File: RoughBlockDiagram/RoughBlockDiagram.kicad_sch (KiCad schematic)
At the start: 11 parts, among them J1 IEC_60320_C14_Receptacle, P1 Conn_Plug_3P_Protected, U1 RaspberryPi, U2 Arduino, U3 Encoder Driver

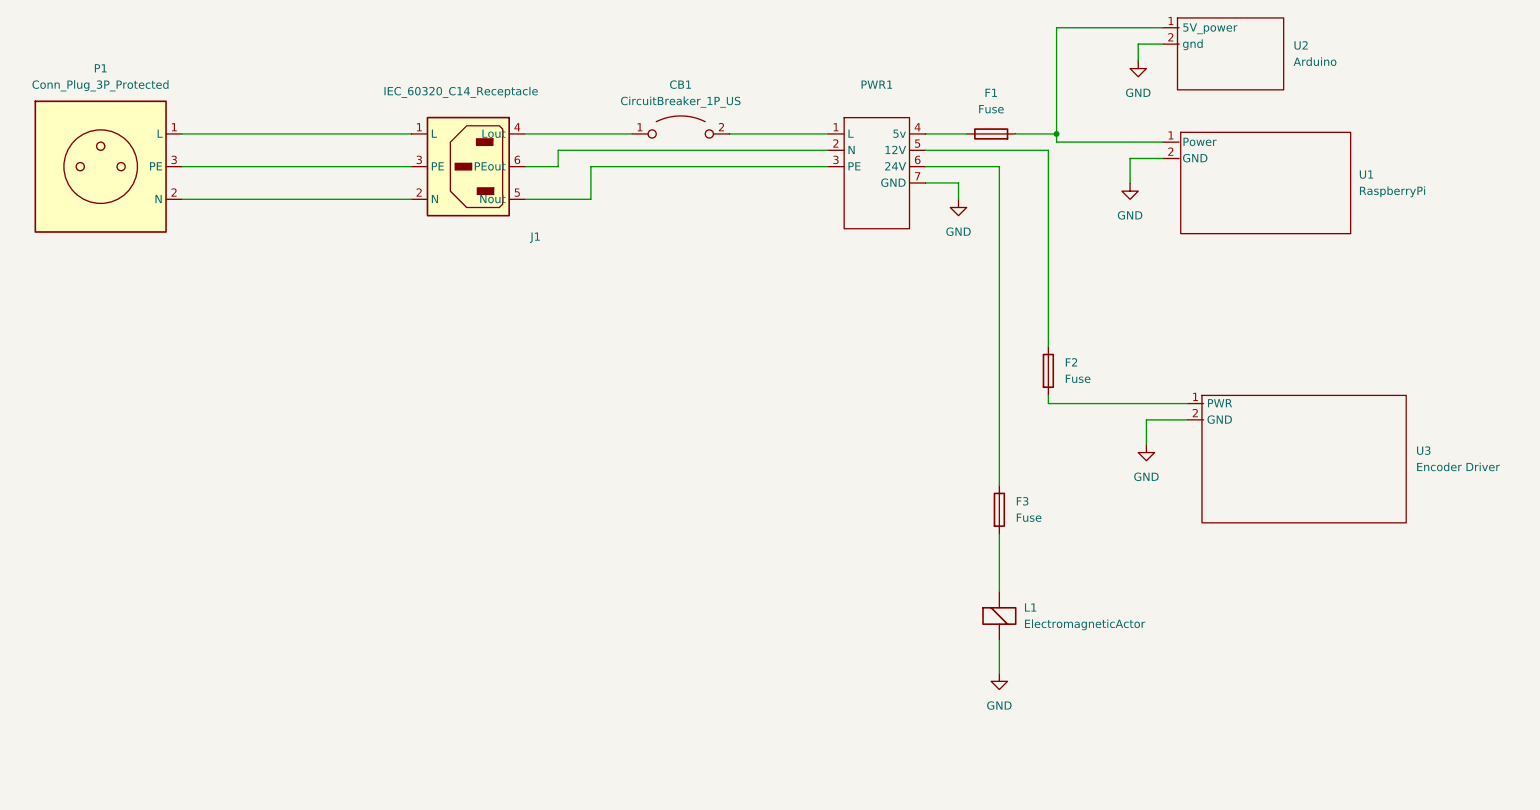
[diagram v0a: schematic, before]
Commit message: Block diagram schematic updated.
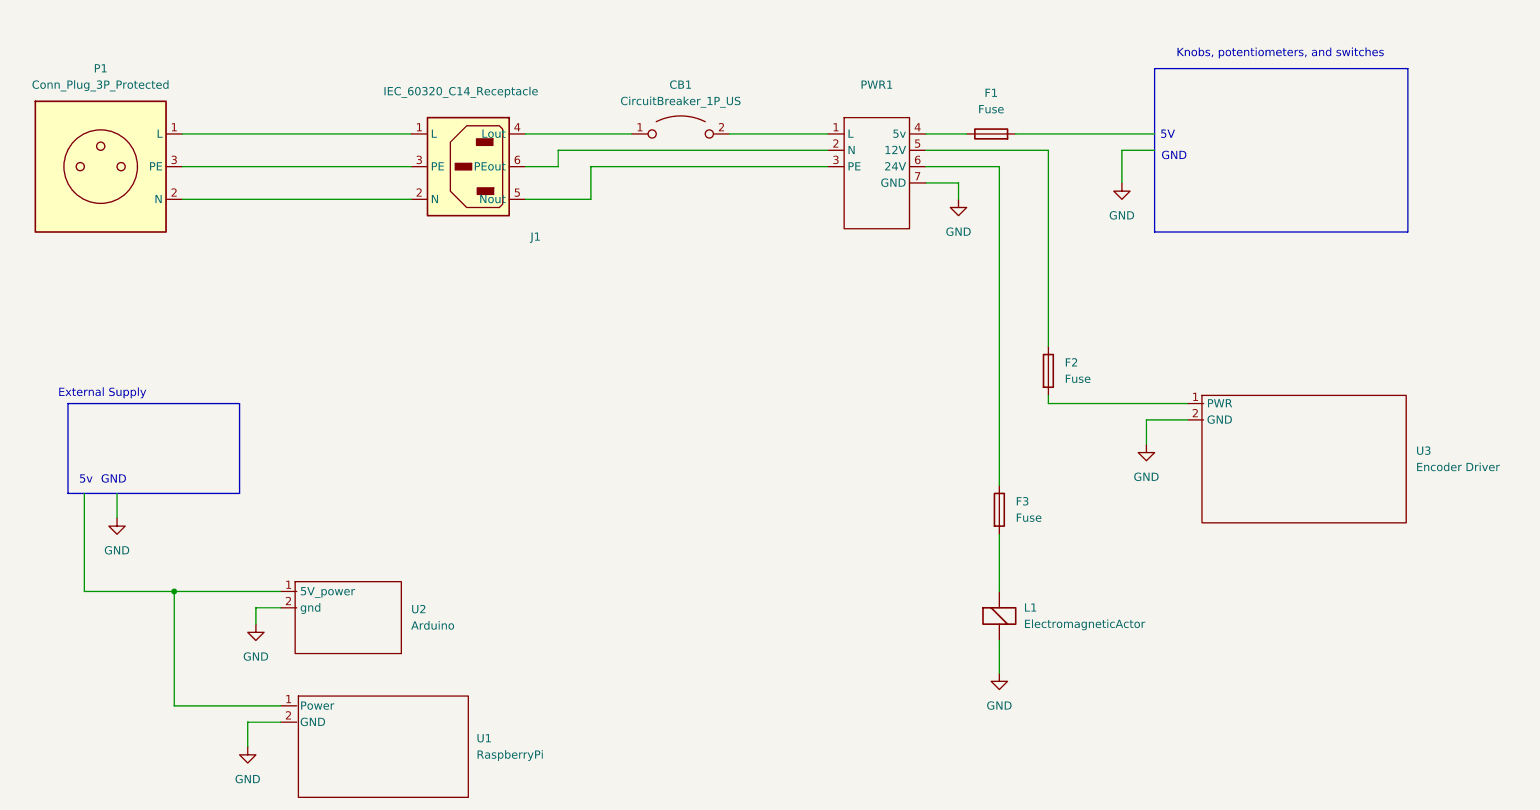
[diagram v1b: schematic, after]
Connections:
- net at U1.1 (Power), U2.1 (5V_power): no longer F1.2
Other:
- note added: "5V"
- note added: "5v"
- note added: "External Supply"
- note added: "GND"
- note added: "Knobs, potentiometers, and switches"
- moved on the sheet: U1, U2
